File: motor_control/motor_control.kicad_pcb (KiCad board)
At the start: 4 copper layers, 75 x 56 mm, 28 parts, among them J1 GPIO, J10 Conn_01x10_Pin, J2 MotA, J3 MotB, J4 MOT_POW, J8 Conn_02x02_Odd_Even, J9 VBUS_OUT, SW1 PU, SW2 PD, SW3 SW_SPDT_312, U1 HC-SR04

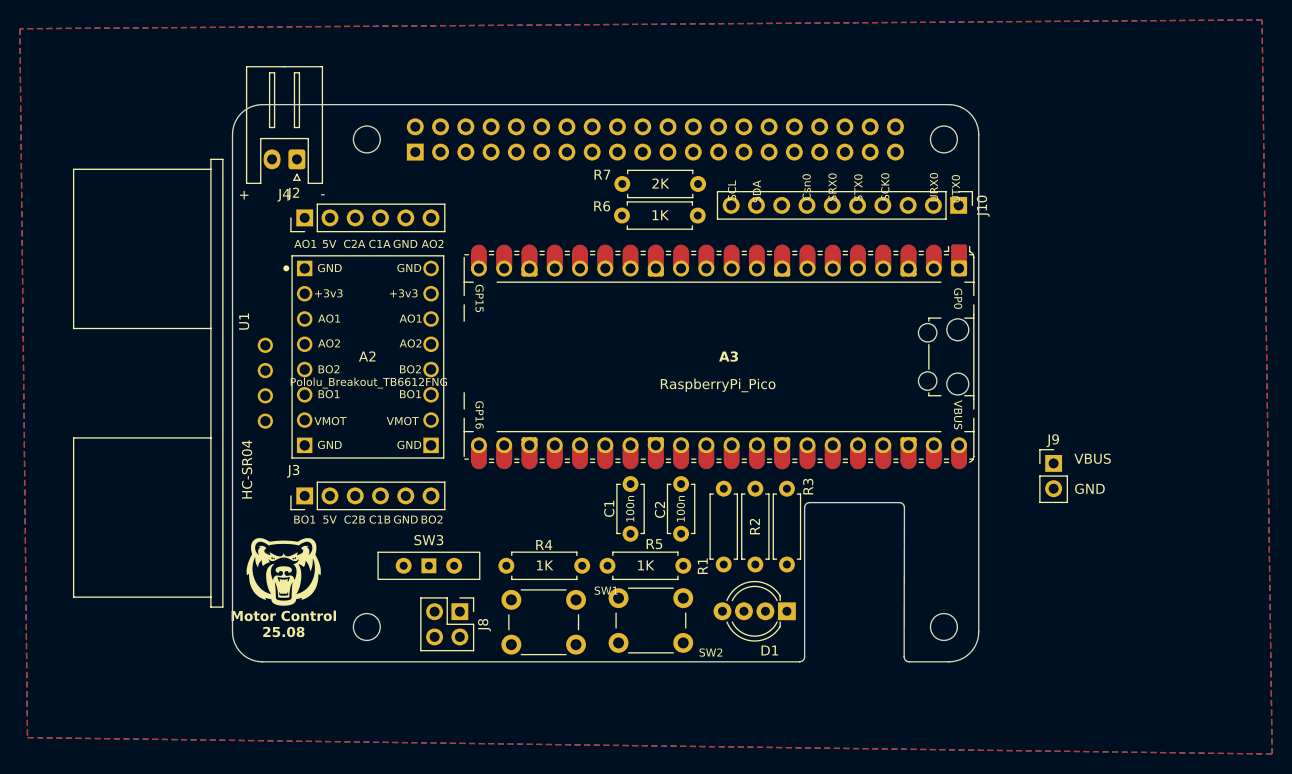
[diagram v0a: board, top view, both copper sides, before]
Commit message: minor update layout
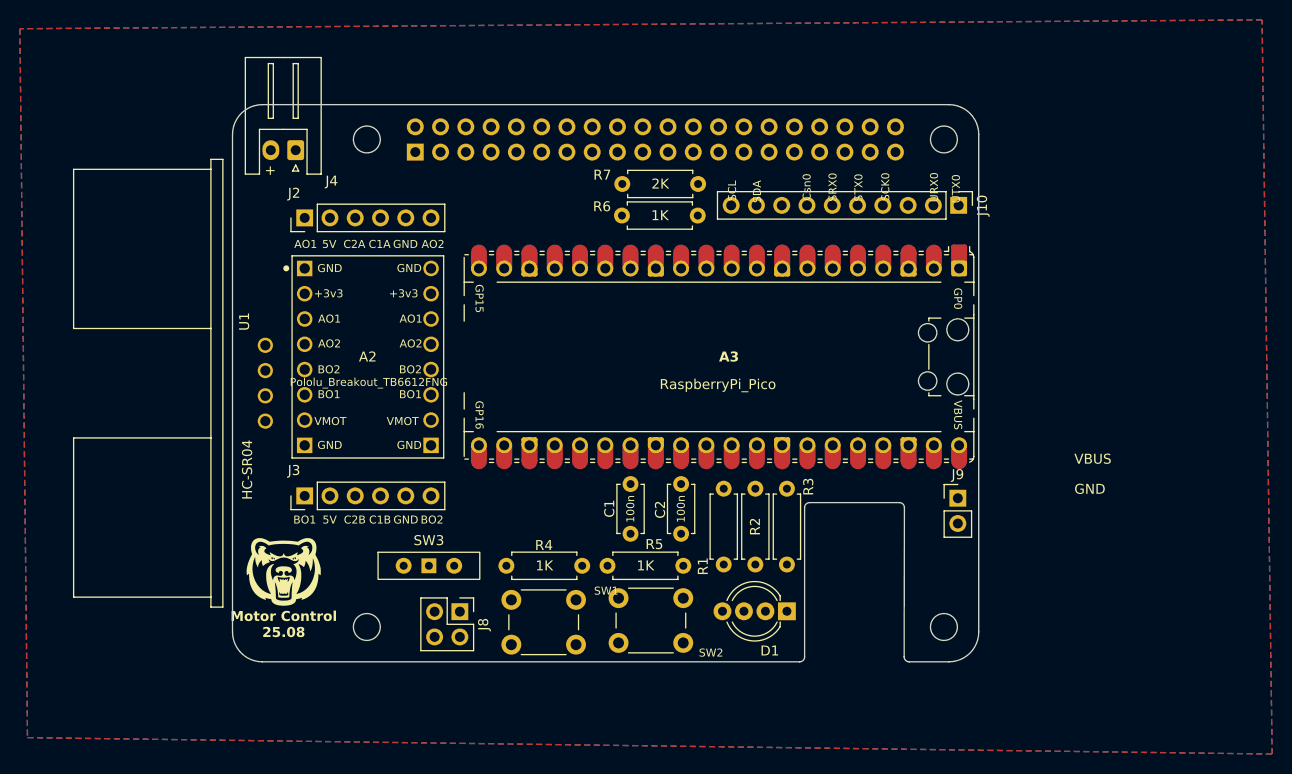
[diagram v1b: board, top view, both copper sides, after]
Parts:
- moved J9 10.2 mm to (162.9, 83.6)
- moved J4 0.93 mm to (96.3, 48.6)
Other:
- board text removed: "-"
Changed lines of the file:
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@@
 	(footprint "Connector_JST:JST_XH_S2B-XH-A_1x02_P2.50mm_Horizontal"
 		(layer "F.Cu")
-		(at 96.475 49.5 180)
+		(at 96.35 48.575 180)
 		(descr "JST XH series connector, S2B-XH-A (http://www.jst-mfg.com/product/pdf/eng/eXH.pdf), generated with kicad-footprint-generator")
 		(tags "connector JST XH horizontal")
 		(property "Reference" "J4"
-			(at 1.25 -3.51 0)
+			(at -3.625 -3.1 0)
 			(layer "F.SilkS")
 			(effects
@@
 	(footprint "Connector_PinHeader_2.54mm:PinHeader_1x02_P2.54mm_Vertical"
 		(layer "F.Cu")
-		(at 172.525 80.06)
+		(at 162.9 83.56)
 		(descr "Through hole straight pin header, 1x02, 2.54mm pitch, single row")
 		(tags "Through hole pin header THT 1x02 2.54mm single row")
@@
 	)
 	(gr_text "+"
-		(at 91.175 53.075 0)
+		(at 93.8 50.6 0)
 		(layer "F.SilkS")
 		(effects
@@
 		)
 	)
-	(gr_text "-"
-		(at 99.075 52.975 0)
-		(layer "F.SilkS")
-		(effects
-			(font
-				(size 1 1)
-				(thickness 0.15)
-			)
-		)
-	)

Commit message: update wiring
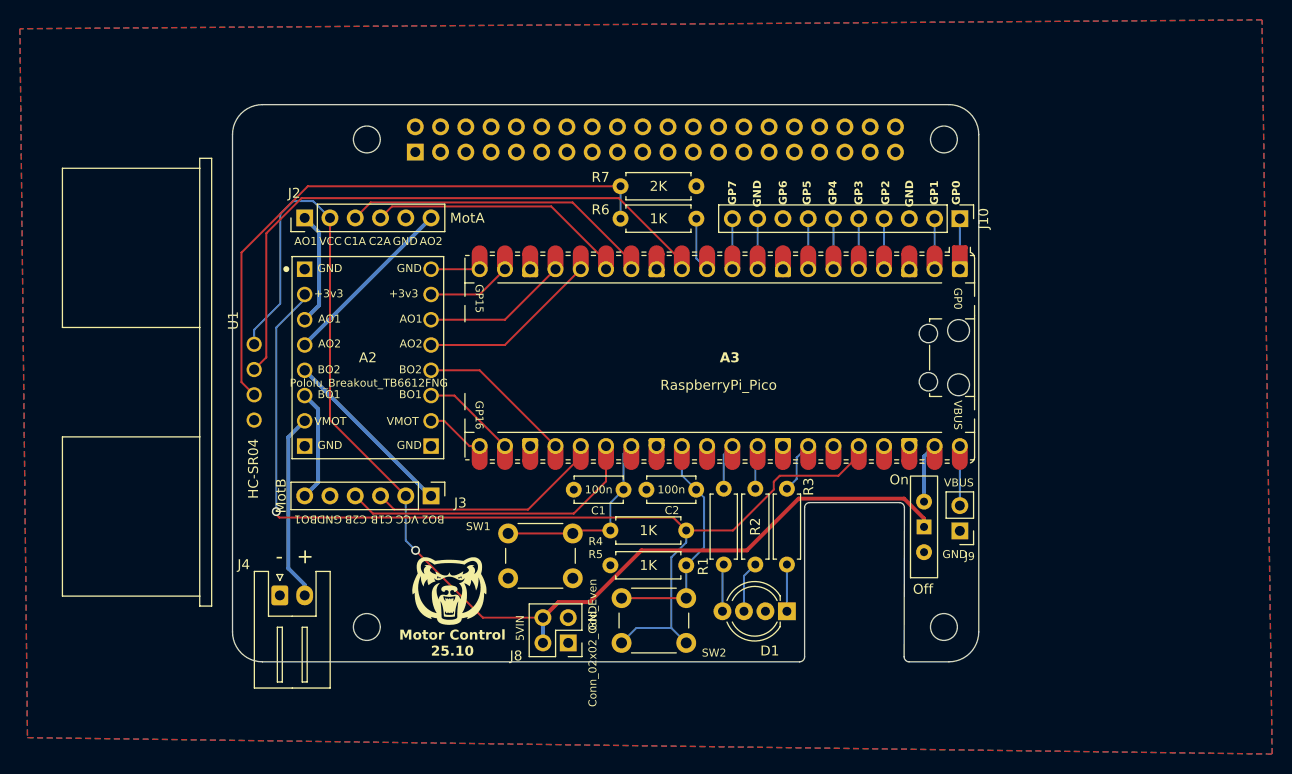
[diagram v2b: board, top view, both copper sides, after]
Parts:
- moved On 49.9 mm to (159.5, 86.4), turned to 90 degrees
- moved J4 44.8 mm to (94.8, 93.3), turned to 0 degrees
- moved G*** 16.8 mm to (111.8, 92.9)
- moved J3 12.7 mm to (110.0, 83.3), turned to -90 degrees
- moved J8 11.3 mm to (123.7, 98.1), turned to 180 degrees
- moved SW1 6.68 mm to (124.2, 91.6)
- moved R4 4.54 mm to (128.0, 86.8), turned to 0 degrees
- moved C1 4.49 mm to (129.3, 82.7), turned to 180 degrees
- moved C2 3.53 mm to (131.6, 82.7), turned to 0 degrees
- moved J9 3.29 mm to (163.1, 86.8), turned to 180 degrees
- moved J10 1.34 mm to (163.1, 55.5)
- moved U1 1.13 mm to (92.2, 71.9)
- moved R6 0.34 mm to (129.0, 55.5)
- moved SW2 0.30 mm to (135.6, 98.1)
- moved R5 0.30 mm to (128.0, 90.3)
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- renumbered SW3 to On
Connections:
- A3 pad 11: /TRIG -> /ECHO
- A3 pad 12: /ECHO -> /TRIG
- A3 pad 14: /C2A -> /C1A
- A3 pad 15: /C1A -> /C2A
- A3 pad 25: /C2B -> /C1B
- A3 pad 26: /C1B -> /C2B
- J9 pad 1: VBUS -> GND
- J9 pad 2: GND -> VBUS
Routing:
- net REG_5V: track 0.00 -> 120.4 mm, vias 0 -> 1
- net +3V3: track 0.00 -> 104.4 mm, vias 0 -> 1
- net /TRIG: track 0.00 -> 60.0 mm
- net Net-(U1-ECHO): track 0.00 -> 58.9 mm
- net /C2B: track 0.00 -> 30.0 mm
- net /C1A: track 1.13 -> 30.8 mm
- net /C2A: track 0.00 -> 26.6 mm
- net /PULLDOWN: track 0.00 -> 23.5 mm
- net /C1B: track 0.00 -> 23.2 mm
- net /PULLUP: track 0.00 -> 19.8 mm
- net VMOT: track 0.00 -> 18.9 mm
- net /STBY: track 0.00 -> 18.2 mm
- net /AO2: track 0.00 -> 18.0 mm
- net /BO2: track 0.00 -> 17.9 mm
- net /BIN1: track 0.00 -> 15.7 mm
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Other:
- board text added: "-"
- board text added: "5VIN"
- board text added: "GP1"
- board text added: "GP2"
- board text added: "GP3"
- board text added: "GP4"
- board text added: "GP5"
- board text added: "GP6"
- board text added: "GP7"
- board text added: "Motor Control 25.10"
- board text added: "Off"
- board text added: "VCC"
- board text removed: "5V"
- board text removed: "Csn0"
- board text removed: "Motor Control 25.08"
- board text removed: "SCK0"
- board text removed: "SCL"
- board text removed: "SDA"
- board text removed: "SRX0"
- board text removed: "STX0"
- board text removed: "URX0"
- board text removed: "UTX0"

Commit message: fix drc issues
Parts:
- A2: value Pololu_Breakout_TB6612FNG -> Pololu_TB6612
- D1: value LED_RKGB -> BGKR
- J8: value Conn_02x02_Odd_Even -> Conn_02x02
- moved J4 1.70 mm to (93.0, 93.4)
- renumbered SW2 to SWD, SW1 to SWU
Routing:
- net VMOT: track 18.9 -> 18.3 mm
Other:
- board text added: "5V"

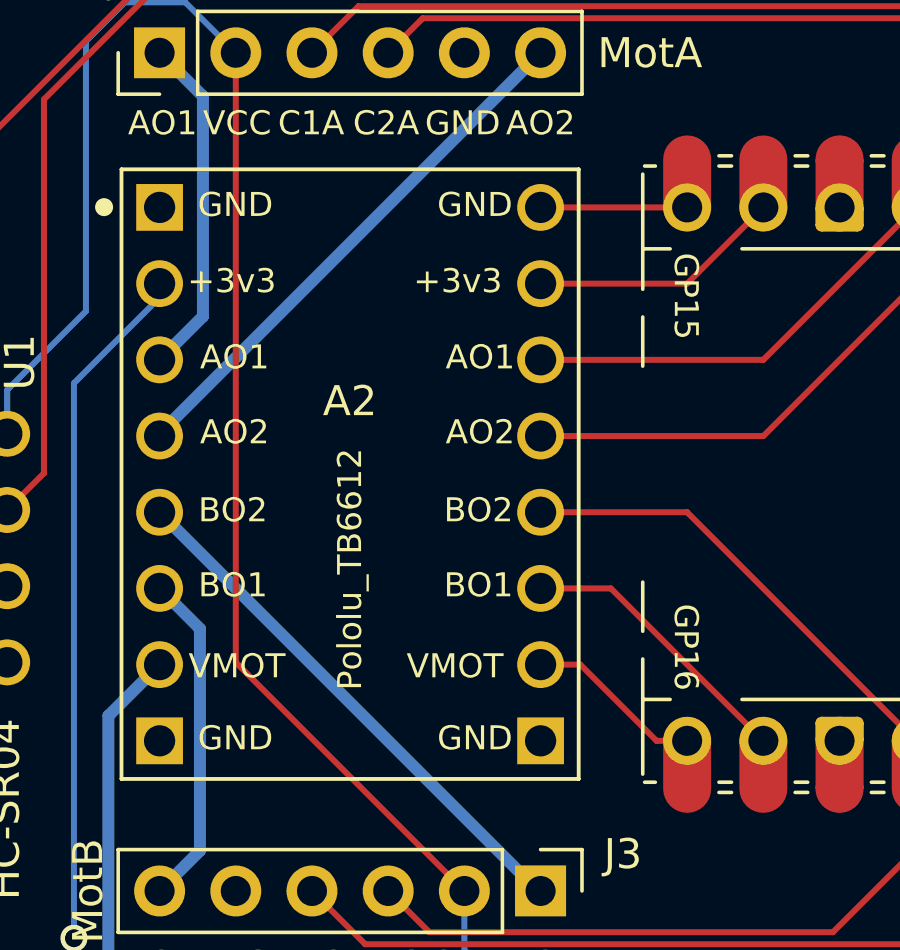
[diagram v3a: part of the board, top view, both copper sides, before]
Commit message: fix motor driver labels
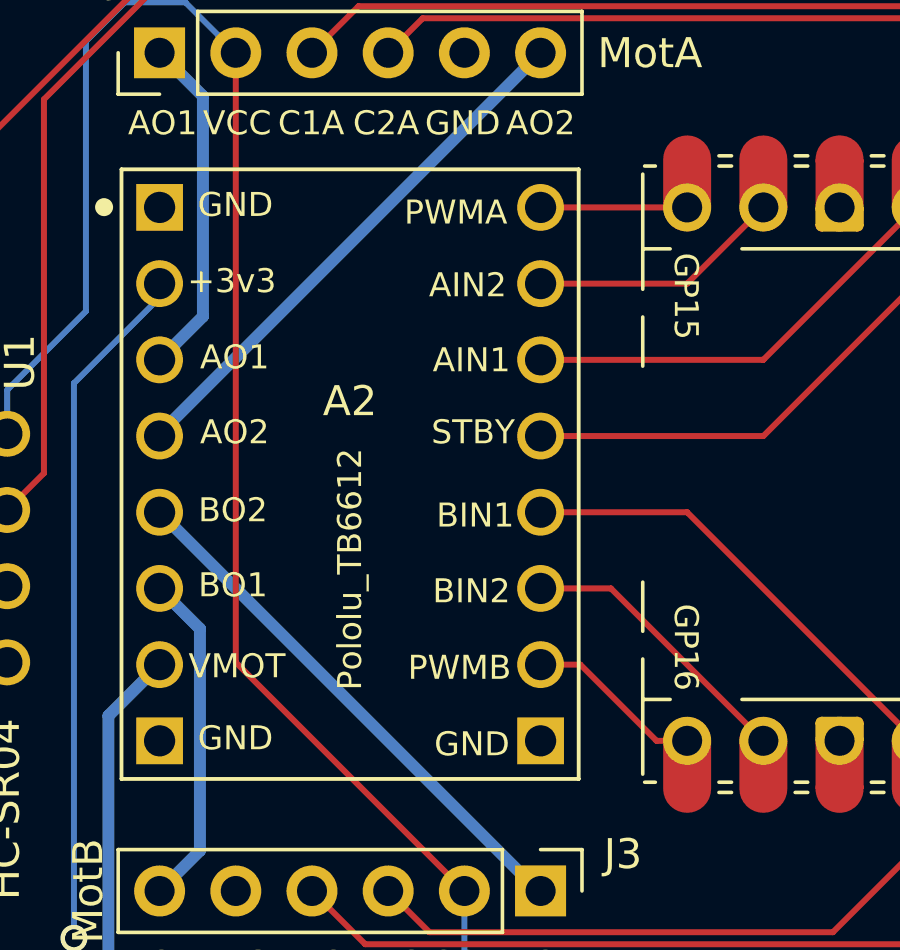
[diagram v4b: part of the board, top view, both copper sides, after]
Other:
- board text added: "AIN1"
- board text added: "AIN2"
- board text added: "BIN1"
- board text added: "BIN2"
- board text added: "PWMA"
- board text added: "PWMB"
- board text added: "STBY"
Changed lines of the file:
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@@
 		)
 	)
-	(gr_text "AO1"
-		(at 109.1 66.0015 0)
-		(layer "F.SilkS")
-		(effects
-			(font
-				(size 0.8 0.8)
-				(thickness 0.1)
-			)
-			(justify right bottom)
-		)
-	)
-	(gr_text "AO2"
+	(gr_text "AIN1"
+		(at 108.95 66.1 0)
+		(layer "F.SilkS")
+		(effects
+			(font
+				(size 0.8 0.8)
+				(thickness 0.1)
+			)
+			(justify right bottom)
+		)
+	)
+	(gr_text "STBY"
 		(at 109.1 68.5 0)
 		(layer "F.SilkS")
@@
 		)
 	)
-	(gr_text "BO1"
-		(at 109.042857 73.6 0)
+	(gr_text "BIN2"
+		(at 108.95 73.8 0)
 		(layer "F.SilkS")
 		(effects
@@
 		)
 	)
-	(gr_text "GND"
-		(at 109.02381 60.9215 0)
+	(gr_text "PWMA"
+		(at 108.85 61.175 0)
 		(layer "F.SilkS")
 		(effects
@@
 		)
 	)
-	(gr_text "+3v3"
-		(at 108.680952 63.4615 0)
+	(gr_text "AIN2"
+		(at 108.825 63.6 0)
 		(layer "F.SilkS")
 		(effects
@@
 		)
 	)
-	(gr_text "BO2"
-		(at 109.042857 71.1 0)
+	(gr_text "BIN1"
+		(at 109.075 71.275 0)
 		(layer "F.SilkS")
 		(effects
@@
 		)
 	)
-	(gr_text "VMOT"
-		(at 108.719048 76.3 0)
+	(gr_text "PWMB"
+		(at 108.975 76.35 0)
 		(layer "F.SilkS")
 		(effects
@@
 	)
 	(gr_text "GND"
-		(at 109.02381 78.7 0)
-		(layer "F.SilkS")
-		(effects
+		(at 108.925 78.9 0)
+		(layer "F.SilkS")
+		(effects
